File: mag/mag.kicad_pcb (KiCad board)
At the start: 2 copper layers, 71.5 x 41 mm, 61 parts, among them K1 кнопка_FSMSM, K2 кнопка_FSMSM, X1 Клеммник_х2

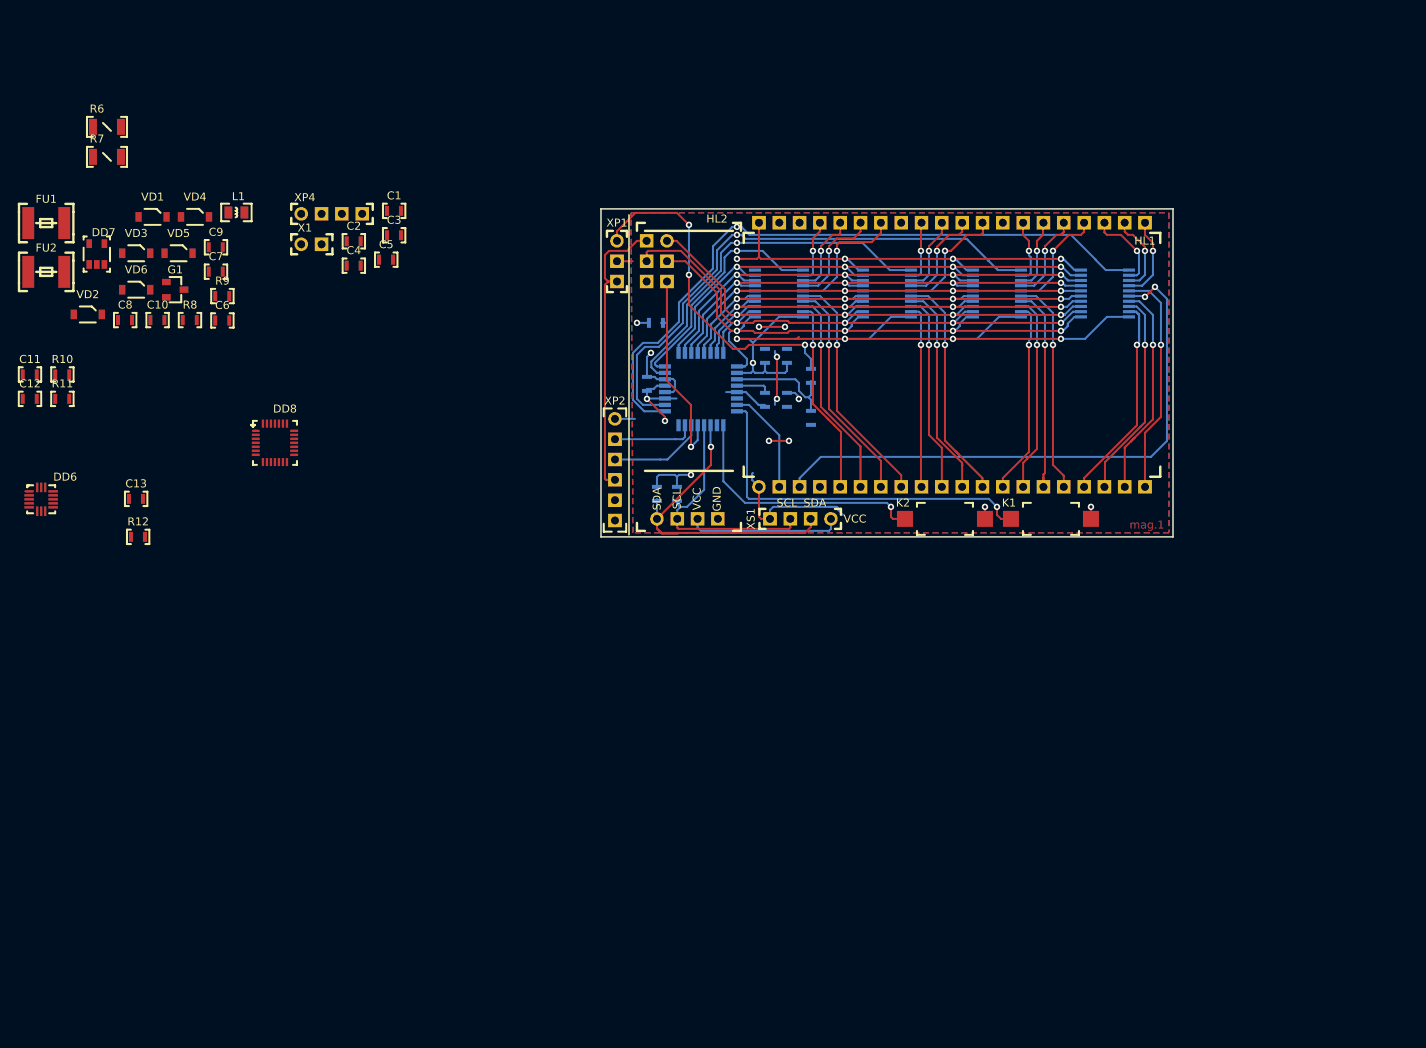
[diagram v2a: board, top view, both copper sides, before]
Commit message: на схеме не отражены внешняя i2c-eeprom
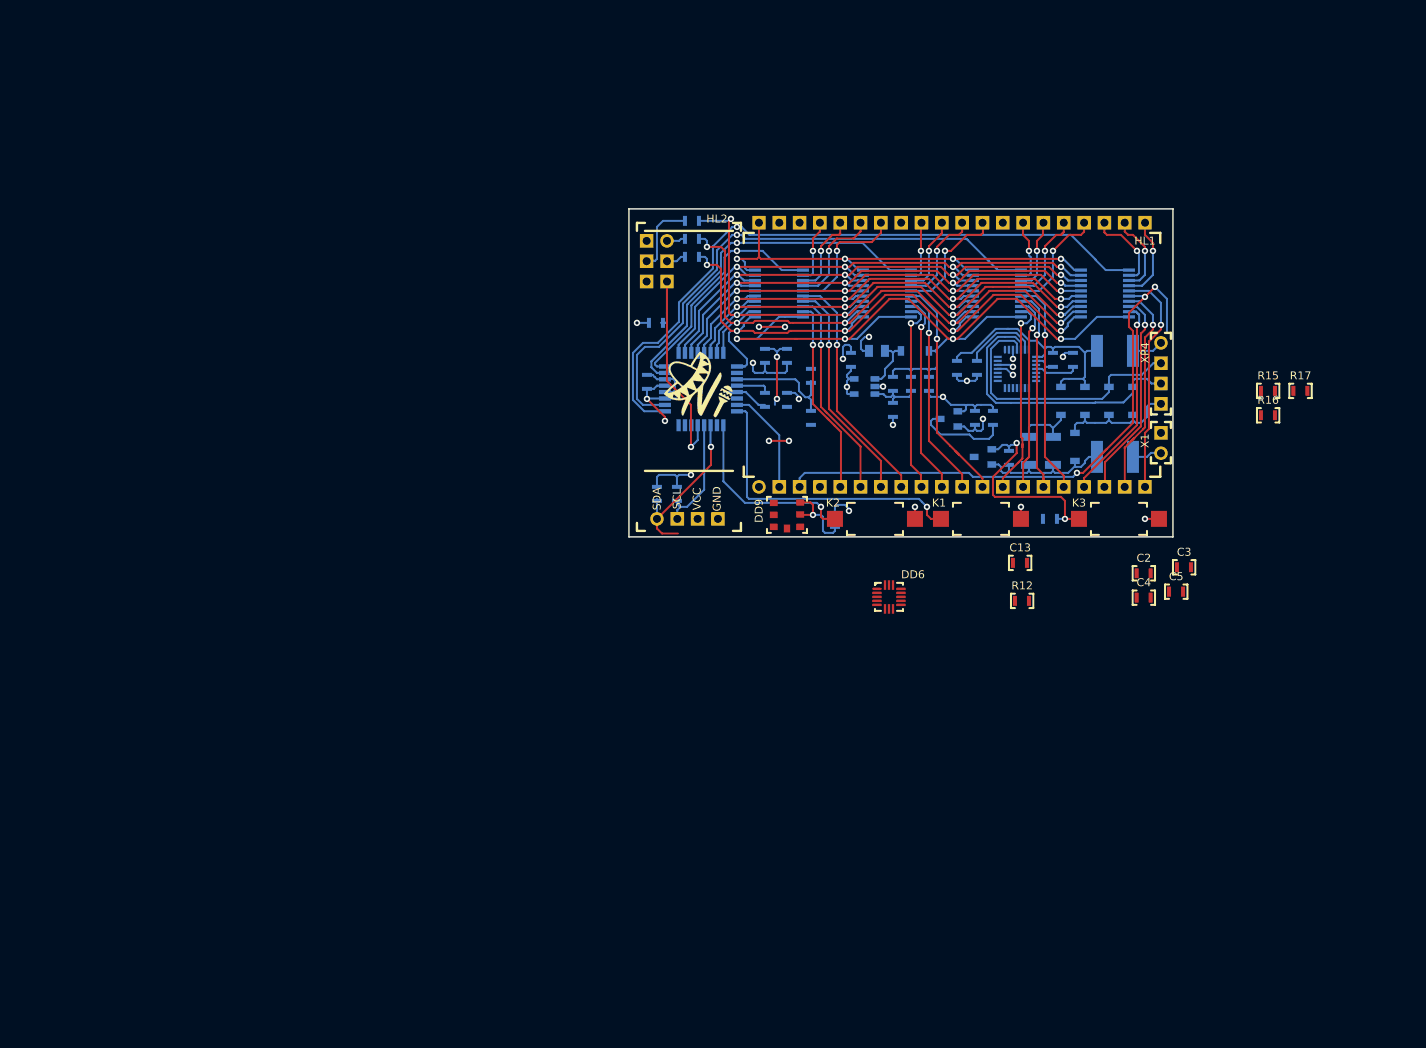
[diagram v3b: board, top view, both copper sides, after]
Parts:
- removed the C1 at (103.8, 61.2)
- removed XP1: Вилка_PLS3, N_X:Розетка_PBS3_вертикальная
- removed XP2: Вилка_PLS6, N_X:Вилка_PLS6_вертикальная
- removed XS1: Розетка_PBS4, N_X:Вилка_PLS4_вертикальная
- added C14: Конденсатор_керамический, N_RLC:Конденсатор_SMD_0603, B.Cu at (127.2, 80.0)
- added DD9: Датчик_bmp180, N_DD:BMP180, F.Cu at (121.2, 80.0)
- added K3: кнопка_FSMSM, N_X:Кнопка_FSMSM, F.Cu at (157.8, 79.0)
- added R13: Резистор_0,065Вт, N_RLC:Конденсатор_SMD_0603, B.Cu at (149.0, 72.2)
- added R14: Резистор_0,065Вт, N_RLC:Конденсатор_SMD_0603, B.Cu at (155.0, 79.0)
- added R15: Резистор_0,065Вт, N_RLC:Конденсатор_SMD_0603, F.Cu at (180.5, 63.0)
- added R16: Резистор_0,065Вт, N_RLC:Конденсатор_SMD_0603, F.Cu at (180.5, 66.0)
- added R17: Резистор_0,065Вт, N_RLC:Конденсатор_SMD_0603, F.Cu at (184.6, 63.0)
- added R18: Резистор_0,065Вт, N_RLC:Конденсатор_SMD_0603, B.Cu at (110.2, 44.0)
- added R19: Резистор_0,065Вт, N_RLC:Конденсатор_SMD_0603, B.Cu at (110.2, 46.2)
- added R20: Резистор_0,065Вт, N_RLC:Конденсатор_SMD_0603, B.Cu at (110.2, 41.8)
- added VT1: Транзистор_полевой_P-канал(IRLML2246TRPBF), N_VD_HL:Транзистор_IRLML6344TR_SOT-23, B.Cu at (145.8, 71.2)
- C1, C10, C11, C12, C6, C7, C8, C9, DD8, FU1, FU2, G1, L1, R10, R11, R6, R7, R8, R9, VD1, VD2, VD3, VD4, VD5, VD6: moved to B.Cu
- G***: moved to F.Cu
- G2: renamed from DD7; moved to B.Cu
- moved FU1 141.2 mm to (164.5, 71.2), turned to 180 degrees
- moved FU2 138.4 mm to (164.5, 58.0), turned to 180 degrees
- moved VD2 131.1 mm to (164.5, 64.2), turned to 90 degrees
- moved R11 127.3 mm to (157.0, 58.2), turned to 270 degrees
- moved R6 127.2 mm to (154.5, 72.2), turned to 90 degrees
- moved R10 124.7 mm to (154.5, 58.2), turned to 270 degrees
- moved R7 123.2 mm to (151.5, 72.2), turned to 90 degrees
- moved VD3 123.0 mm to (161.5, 64.2), turned to 90 degrees
- moved C12 119.4 mm to (145.0, 59.2), turned to 270 degrees
- moved VD1 118.8 mm to (158.5, 64.2), turned to 90 degrees
- moved C11 116.8 mm to (142.5, 59.2), turned to 270 degrees
- moved VD4 113.7 mm to (157.2, 70.0), turned to 270 degrees
- moved VD5 111.8 mm to (155.5, 64.2), turned to 270 degrees
- moved C13 110.8 mm to (149.5, 84.5)
- moved R12 110.8 mm to (149.8, 89.2)
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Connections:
- C1 pad 1: /VCC -> /VCC_bat
- C1 pad 2: /GND -> /gnd
- C10 pad 1: /power/5V_out -> /5V
- C2 pad 1: /VCC -> /VCC_bat
- C2 pad 2: /GND -> /gnd
- C3 pad 1: /VCC -> /VCC_bat
- C3 pad 2: /GND -> /gnd
- C4 pad 1: /VCC -> /VCC_bat
- C4 pad 2: /GND -> /gnd
- C5 pad 2: /GND -> /gnd
- C6 pad 1: /power/BATT_out -> /VCC_bat
- C7 pad 1: /power/BATT_out -> /VCC_bat
- C8 pad 1: /power/5V_out -> /5V
- DD1 pad 18: /VCC -> /VCC_bat
- DD1 pad 26: Net-(DD1-Pad26) -> /PC3
- DD1 pad 3: /GND -> /gnd
- DD1 pad 30: /MC_RX -> /TX(MOSI)
- DD1 pad 31: /MC_TX -> /RX(MISO)
- DD1 pad 4: /VCC -> /VCC_bat
- DD1 pad 5: /GND -> /gnd
- DD1 pad 6: /VCC -> /VCC_bat
- DD2 pad 20: /VCC -> /5V
- DD3 pad 20: /VCC -> /5V
- DD4 pad 20: /VCC -> /5V
- DD5 pad 20: /VCC -> /5V
- FU1 pad 2: /power/BATT_out -> /power/Bat_in+
- G1 pad 3: /power/BATT_out -> /VCC_bat
- G2 pad 4: /power/BATT_out -> /VCC_bat
- G2 pad 5: /power/BATT_out -> /VCC_bat
- HL2 pad 3: /VCC -> /3V
- HL2 pad 4: /GND -> /gnd
- L1 pad 1: /power/BATT_out -> /VCC_bat
- R1 pad 1: /VCC -> /VCC_bat
- R2 pad 1: /VCC -> /VCC_bat
- R3 pad 1: /VCC -> /VCC_bat
- R4 pad 1: Net-(R4-Pad1) -> /VCC_bat
- R4 pad 2: Net-(R4-Pad2) -> /ADC6
- R5 pad 1: Net-(R5-Pad1) -> /ADC6
- R5 pad 2: Net-(R5-Pad2) -> /gnd
- R6 pad 1: /power/BATT_out -> /power/Bat_in+
- R7 pad 1: /power/BATT_out -> /power/Bat_in+
- R8 pad 1: /power/5V_out -> /5V
- VD4 pad 2: /power/BATT_out -> /power/Bat_in+
- VD6 pad 2: /power/5V_out -> /5V
- XP3 pad 1: /PB3_MOSI -> Net-(R18-Pad2)
- XP3 pad 2: /VCC_prog -> Net-(XP3-Pad2)
- XP3 pad 3: /PB5_SCK -> Net-(R19-Pad2)
- XP3 pad 4: /PB4_MISO -> Net-(R20-Pad2)
- XP3 pad 6: /GND -> /gnd
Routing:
- net /VCC: track 132.3 -> 9.64 mm, vias 9 -> 2
- net /5V: track 0.00 -> 100.7 mm, vias 0 -> 4
- net /gnd: track 0.00 -> 56.6 mm, vias 0 -> 11
- net /VCC_prog: track 36.7 -> 0.00 mm
- net /USB_D-: track 0.00 -> 36.3 mm
- net /USB_D+: track 0.00 -> 34.6 mm
- net /USBtoUART/USB_pwr: track 0.00 -> 32.9 mm
- net /GND: track 109.0 -> 81.9 mm, vias 14 -> 12
- net Net-(K3-Pad1): track 0.00 -> 26.2 mm, vias 0 -> 2
- net /SDA: track 41.9 -> 21.1 mm
- net /power/Bat_in+: track 0.00 -> 18.5 mm
- net /SCL: track 31.0 -> 14.8 mm
- net /3V: track 0.00 -> 15.2 mm, vias 0 -> 2
- net /MC_RX: track 12.1 -> 0.00 mm
- net /MC_TX: track 10.3 -> 0.00 mm
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- added copper zone on In2.Cu, net /VCC_bat
- added copper zone on In1.Cu, net /gnd
- removed copper zone on B.Cu, net /GND
- removed copper zone on F.Cu, net /VCC
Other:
- board size 71.5 x 41 mm -> 68 x 41 mm
- copper layers 2 -> 4
- rule pad_to_mask_clearance: 0.02 -> 0.05
- rule solder_mask_min_width: 0.02 -> 0.2
- board text removed: "BAT"
- board text removed: "PR"
- board text removed: "RX"
- board text removed: "TX"

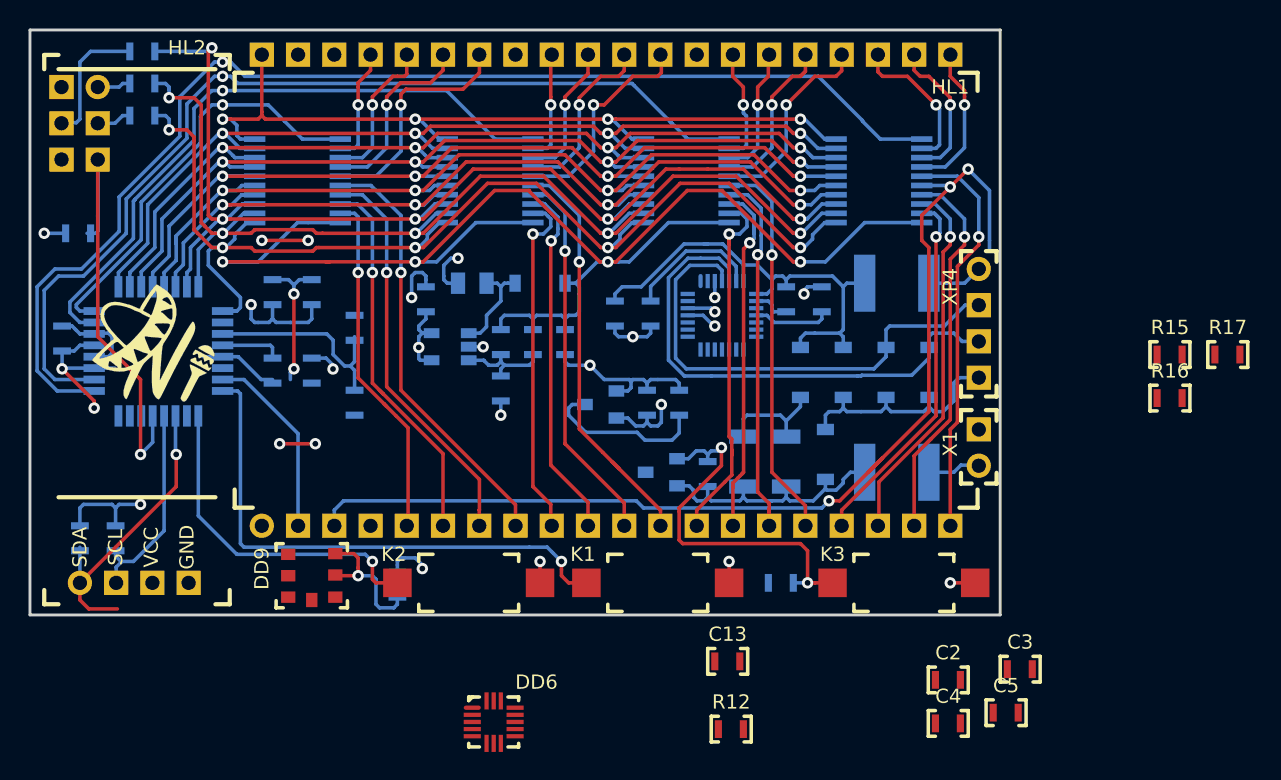
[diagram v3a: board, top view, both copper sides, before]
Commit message: закончена около-боевая разводка, на плате оставлены штыревые разъемы
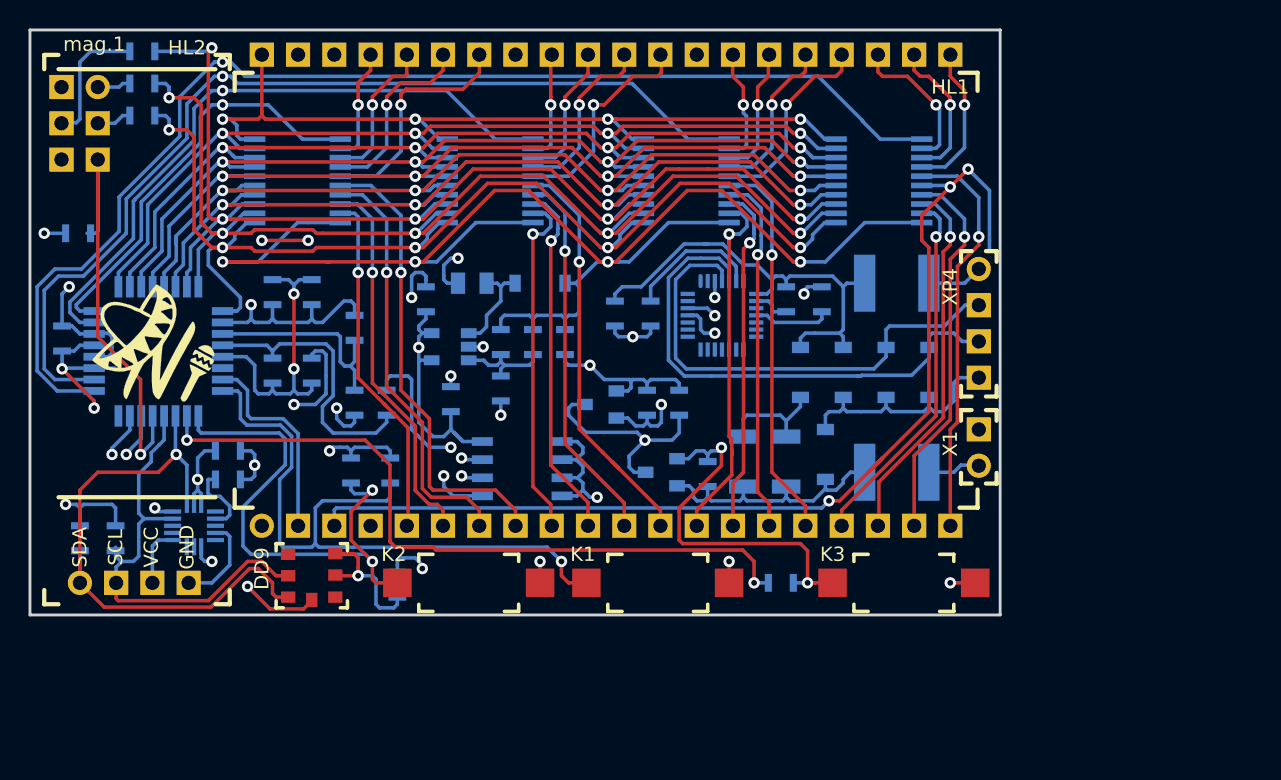
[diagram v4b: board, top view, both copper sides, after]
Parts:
- removed the C2 at (165.0, 85.8)
- removed the C3 at (170.0, 85.0)
- removed the C4 at (165.0, 88.8)
- removed the C5 at (169.0, 88.1)
- added C15: Конденсатор_керамический, N_RLC:Конденсатор_SMD_0603, B.Cu at (131.0, 67.0)
- added DD7: Память_eeprom_AT24C512C, N_DD:SO-8, B.Cu at (136.0, 71.0)
- C13, DD6, R12, R15, R16, R17: moved to B.Cu
- C2, C3, C4, C5: value 10мкФ_0603 -> Конденсатор_керамический
- moved R17 58.2 mm to (126.5, 67.2), turned to 90 degrees
- moved R16 56.7 mm to (124.0, 70.2), turned to 270 degrees
- moved R15 54.2 mm to (126.8, 70.2), turned to 270 degrees
- moved R12 39.4 mm to (114.5, 71.8)
- moved C13 38.0 mm to (114.5, 69.8)
- moved DD6 25.1 mm to (113.0, 75.0)
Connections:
- net /PD2 renamed Net-(DD1-Pad32)
- C2 pad 1: /VCC -> /VCC_bat
- C2 pad 2: /GND -> /gnd
- C3 pad 1: /VCC -> /VCC_bat
- C3 pad 2: /GND -> /gnd
- C4 pad 1: /VCC -> /VCC_bat
- C4 pad 2: /GND -> /gnd
- C5 pad 2: /GND -> /gnd
- DD1 pad 21: /GND -> /gnd
- DD2 pad 10: /GND -> /gnd
- DD3 pad 10: /GND -> /gnd
- DD4 pad 10: /GND -> /gnd
- DD5 pad 10: /GND -> /gnd
- HL1 pad 1: /GND -> /gnd
- HL1 pad 40: /GND -> /gnd
- K1 pad 2: /GND -> /gnd
- K2 pad 2: /GND -> /gnd
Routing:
- net /gnd: track 56.6 -> 170.5 mm, vias 11 -> 26
- net /GND: track 81.9 -> 3.25 mm, vias 12 -> 2
- net /SDA: track 21.1 -> 82.7 mm, vias 1 -> 2
- net /SCL: track 14.8 -> 70.4 mm, vias 0 -> 1
- net /RX(MISO): track 2.21 -> 54.9 mm, vias 1 -> 2
- net /PC3: track 0.00 -> 50.6 mm, vias 0 -> 2
- net /TX(MOSI): track 2.00 -> 50.9 mm, vias 1 -> 2
- net /VCC_bat: track 34.6 -> 79.3 mm, vias 4 -> 9
- net /3V: track 15.2 -> 37.2 mm, vias 2 -> 5
- net /AREF: track 4.31 -> 19.8 mm
- net /PC2: track 23.6 -> 37.1 mm, vias 1 -> 2
- net /PC1: track 37.8 -> 47.5 mm
- net /VCC: track 9.64 -> 0.00 mm, vias 2 -> 0
- net Net-(DD6-Pad10): track 0.00 -> 5.31 mm
- net /Out14: track 30.2 -> 32.8 mm
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- added copper zone on In2.Cu, net /3V

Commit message: сформированны файлы для заказа
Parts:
- removed the G*** at (110.8, 62.8)
- added G***: LOGO, N_ICO:el-nikitos_29x10, F.Cu at (149.0, 69.0)
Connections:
- DD7 pad 5: /SCL -> /SDA
- DD7 pad 6: /SDA -> /SCL
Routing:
- net /5V: track 100.7 -> 97.3 mm
- net /PB5_SCK: track 83.0 -> 79.6 mm
- net /PB0: track 62.9 -> 59.6 mm
- net /PB1: track 64.2 -> 60.9 mm
- net /PB3_MOSI: track 82.8 -> 79.4 mm
- net /PB2: track 65.6 -> 62.3 mm
- net /PB4_MISO: track 80.6 -> 77.5 mm
- net /PD7: track 64.0 -> 61.5 mm
- net /SDA: track 82.7 -> 84.4 mm
- net /PD6: track 65.1 -> 63.4 mm
- net /gnd: track 170.5 -> 169.1 mm
- net /PD5: track 66.2 -> 65.3 mm
- net /SCL: track 70.4 -> 71.1 mm
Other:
- board text added: "mag.1(10/19)"
- board text removed: "mag.1"
